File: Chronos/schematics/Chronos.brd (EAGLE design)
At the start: 61.6 x 100 mm, 72 parts, among them IC1 REG1117, IC4 QUAD_OPAMPD, Q301 BC846, Q701 BC846, U1 STM32F10XRXT6

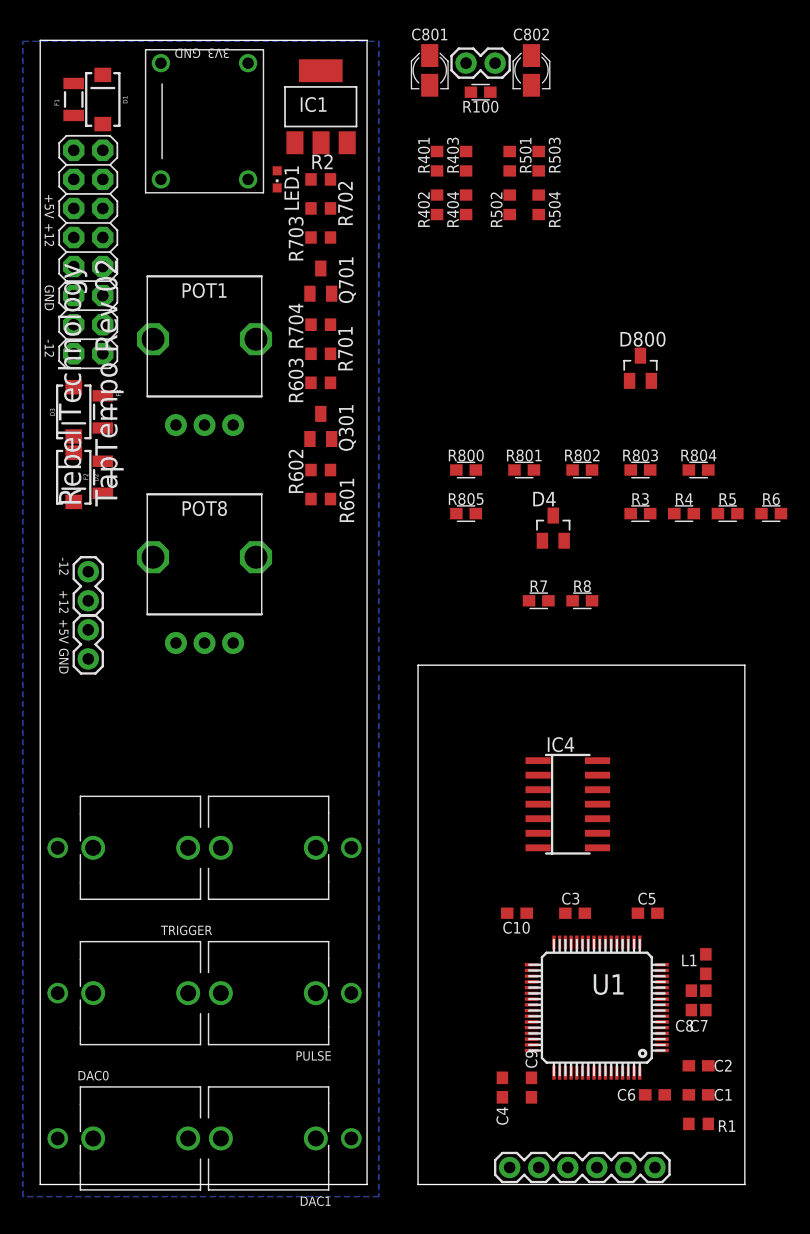
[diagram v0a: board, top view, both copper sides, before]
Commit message: replaced Chronos with TapTempoMk2
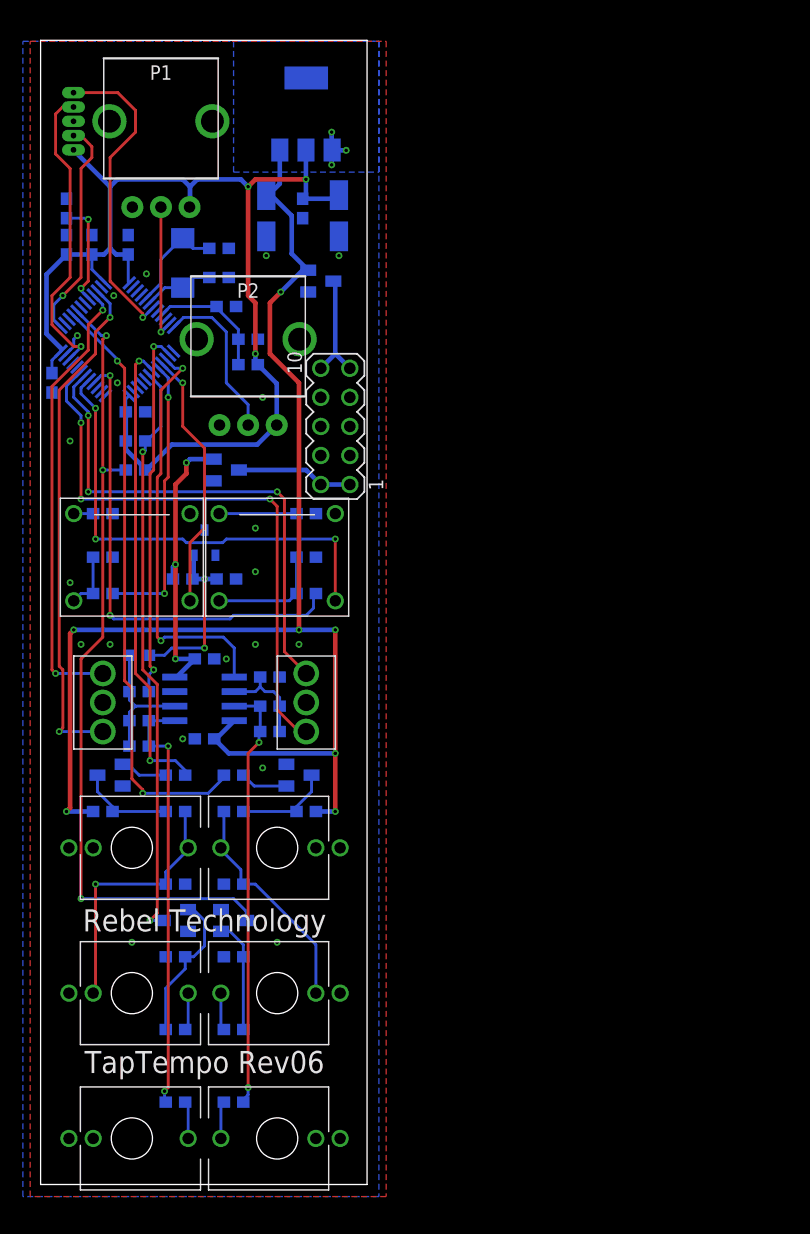
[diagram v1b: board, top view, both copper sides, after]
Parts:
- removed C801, C802: 10u, resistor:PANASONIC_A
- removed D1, D2, D3: (no value), SparkFun:SMA-DIODE
- removed D4, D800: BAT54S, diode:SOT23
- removed DAC0: THONKICONN, Rebel:THONKICONN
- removed F1, F2, F3: PTCSMD, SparkFun:PTC-1206
- removed IC4: QUAD_OPAMPD, adafruit:SO14
- removed JP1: (no value), SparkFun:1X06
- removed JP21, JP22, JP23: (no value), SparkFun:1X02
- removed LED1: (no value), led:CHIPLED_0603
- removed POT1, POT8: POT-ALPS-RK09L1140, Rebel:POT-ALPS-RK09L1140
- removed Q301, Q701: BC846, transistor:SOT23
- removed R100: 150R, Rebel:0603
- removed R401: 270k, resistor:R0603
- removed R402, R502: 100k, resistor:R0603
- removed R403, R503: 68k, resistor:R0603
- removed R404, R504: 100R, resistor:R0603
- removed R501: 470k, resistor:R0603
- removed R601: 100K, resistor:R0603
- removed R602: 1M, resistor:R0603
- removed R603: 10K, resistor:R0603
- removed R701, R702, R704: 1K, resistor:R0603
- removed R703: 100, resistor:R0603
- removed R800, R802: 240k, Rebel:0603
- removed R801: 100k, Rebel:0603
- removed R803: 68k, Rebel:0603
- removed R804: 1k, Rebel:0603
- removed R805: 100R, Rebel:0603
- removed U$1: 5GTH9, SWITCH-5GTH9:5GTH9
- removed U$2: M08X2, SparkFun:2X8
- removed U$3: (no value), Rebel:RT-LOGO-35MM-BL
- added C11, C13, C14, C16, C18, C19: 100n, Rebel:C0603
- added C12, C17: 10u, Rebel:153CLV-0405
- added C15: 1u, Rebel:C0603
- added DAC2: THONKICONN, Rebel:THONKICONN
- added IC2: TL072D, linear:SO08
- added IC3: LM4040B10, texas:DBZ_R-PDSO-G3
- added P1, P2: POT-ALPS-RK09L1140, Rebel:POT-ALPS-RK09L1140
- added PUSH1, PUSH2: 5GTH9, SWITCH-5GTH9:5GTH9
- added Q4: SI2309CDS, transistor-small-signal:SOT23
- added Q5: BSS123, transistor-small-signal:SOT23
- added R10, R13, R16, R17: 1K, Rebel:0603
- added R11: 100K, Rebel:0603
- added R12, R26, R27: 100R, Rebel:0603
- added R14: 1M, Rebel:0603
- added R15, R9: 10K, Rebel:0603
- added R18, R19: 150R, Rebel:0603
- added R20, R23: 1k, Rebel:0603
- added R21: 510R, Rebel:0603
- added R22: 6k8, Rebel:0603
- added R24: 3k3, Rebel:0603
- added R25: 2k, Rebel:0603
- added SV1: (no value), con-lstb:MA05-2
- added SW1, SW2: SUB-MIN-SPDT, Rebel:SUB-MIN-SPDT
- added T1, T2, T3, T4: BC846, transistor:SOT23
- added X1: 53048-05, con-molex:53048-05
- added Y1: 8MHz, Seeed-OPL-crystal-osctllator:X2-SMD-5.0X3.2X1.3MM
- C1: value 1u -> 2u2; device resistor:C0603 -> Rebel:C0603
- C10, C2, C5, C9: device resistor:C0603 -> Rebel:C0603
- C3: value 2u2 -> 4.7u; device resistor:C0603 -> Rebel:C0603
- C4: value 2u2 -> 100n; device resistor:C0603 -> Rebel:C0603
- C6, C8: value 100n -> 20pF; device resistor:C0603 -> Rebel:C0603
- C7: value 1u -> 100n; device resistor:C0603 -> Rebel:C0603
- IC1: value REG1117 -> TLV1117-33CDCY
- L1: device Rebel:0603@1 -> Rebel:0603
- R1: value 10K -> 1K; device resistor:R0603 -> Rebel:0603
- R2: device resistor:R0603 -> Rebel:0603
- R3: value 100k -> 100K
- R4: value 240k -> 100R
- R5: value 240k -> 1K
- R6: value 68k -> 1M
- R7: value 1k -> 10K
- R8: value 100R -> 1K
- U1: value STM32F10XRXT6 -> STM32F100CBT6B; device stm32:TQFP64 -> Rebel:QFP50P900X900X160-48N
- moved C6 83.2 mm to (17.8, 82.9), flipped to the bottom
- moved C9 83.1 mm to (6.67, 83.2), flipped to the bottom, turned to 90 degrees
- moved C2 78.1 mm to (18.4, 77.8), flipped to the bottom, turned to 180 degrees
- moved C1 76.9 mm to (20.3, 74.9), flipped to the bottom, turned to 180 degrees
- moved C8 75.5 mm to (17.8, 80.3), flipped to the bottom, turned to 180 degrees
- moved C3 73.4 mm to (4.45, 83.2), flipped to the bottom, turned to 90 degrees
- moved U1 71.9 mm to (8.89, 74.9), flipped to the bottom, turned to 315 degrees
- moved C7 71.6 mm to (10.5, 68.6), flipped to the bottom, turned to 180 degrees
- moved L1 65.9 mm to (20.3, 72.7), flipped to the bottom, turned to 0 degrees
- moved C10 61.6 mm to (3.17, 71.1), flipped to the bottom, turned to 270 degrees
- moved R6 60.9 mm to (19.1, 21.0), flipped to the bottom
- moved R3 57.4 mm to (19.1, 14.6), flipped to the bottom, turned to 180 degrees
- moved C5 56.9 mm to (7.62, 55.9), flipped to the bottom, turned to 180 degrees
- moved R2 55.3 mm to (25.4, 33.7), flipped to the bottom
- moved R5 54.0 mm to (19.1, 27.3), flipped to the bottom, turned to 180 degrees
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- renumbered PULSE to TEMPO2, TRIGGER to TEMPO1, TRIGGER1 to TR2, TRIGGER2 to TR1
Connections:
- removed net +5V: C801.+, D1.C, F1.2, IC1.3, JP22.1
- removed net ADC3: U1.9
- removed net ADC4: R8.1, R805.1, U1.15
- removed net ADC5: U1.16
- removed net ADC6: U1.8
- removed net DI0: Q301.3, R603.2, U1.50
- removed net DI1: U1.28
- removed net DO0: R701.1, U1.57
- removed net DO1: U1.27
- removed net N$19: LED1.C, R2.2
- removed net N$29: DAC1.P$2
- removed net N$33: IC4.2, R800.2, R801.2, R802.2, R803.1
- removed net N$35: R703.2, R704.2, TEMPO2.P$3
- removed net N$36: D800.3, R804.1, R805.2
- removed net N$44: F1.1, U$2.11, U$2.12
- removed net N$45: F2.1, U$2.10, U$2.9
- removed net N$8: DAC0.P$2
- removed net PA0: U1.14
- removed net PA10: U1.43
- removed net PA11: U1.44
- removed net PA12: U1.45
- removed net PA3: U1.17
- removed net PA4: R403.2, U1.20
- removed net PA5: R503.2, U1.21
- removed net PA6: U1.22
- removed net PA7: U1.23
- removed net PA8: U1.41
- removed net PA9: U1.42
- removed net PB0: U1.26
- removed net PB10: U1.29
- removed net PB11: U1.30
- removed net PB12: U1.33
- removed net PB13: U1.34
- removed net PB14: U1.35
- removed net PB15: U1.36
- removed net PB4: U1.56
- removed net PB6: U1.58
- removed net PB7: U1.59
- removed net PB8: U1.61
- removed net PB9: U1.62
- removed net PC10: U1.51
- removed net PC11: U1.52
- removed net PC12: U1.53
- removed net PC13: U1.2
- removed net PC14: U1.3
- removed net PC15: U1.4
- removed net PC4: U1.24
- removed net PC5: U1.25
- removed net PC6: U1.37
- removed net PC7: U1.38
- removed net PC8: U1.39
- removed net PC9: U1.40
- removed net PD2: U1.54
- removed net PE2: U$1.4
- removed net PE3: R100.2
- removed net PE5: U$1.-2
- removed net SWO: JP1.6, U1.55
- removed net VCAP_1: C3.1, U1.31
- removed net VCAP_2: C4.1, U1.47
- new net BOOT1: U1.20
- new net CV_REF: C16.1, IC3.2, R21.2, R22.2
- new net DAC1: R23.2, U1.14
- new net DAC2: IC2.5, U1.15
- new net LED1: PUSH1.+3, U1.16
- new net LED2: PUSH2.+3, U1.29
- new net N$15: R4.2, R5.2, TEMPO2.P$2, TR2.P$3
- new net N$16: Q5.3, SV1.1, SV1.2
- new net N$17: C5.1, PUSH1.4, R17.1
- new net OSC_IN: C6.1, U1.5, Y1.1
- new net PUSH1: R17.2, U1.17
- new net PUSH2: R16.2, U1.28
- new net SW1A: SW1.3, U1.45
- new net SW1B: SW1.1, U1.46
- new net SW2A: SW2.3, U1.30
- new net SW2B: SW2.1, U1.31
- new net TEMPO1: R15.2, T4.3, U1.19
- new net TEMPO2: R7.2, T2.3, U1.41
- new net TR1: R8.1, U1.18
- new net TR2: R1.1, U1.40
- net +12V: now also C12.+, C19.1, IC1.3, IC2.8, Q4.2, R10.1, R2.1; no longer D2.C, F2.2, IC4.4, JP23.1, POT1.3, POT8.3, R702.1
- net +3V3: now also C11.1, C15.1, C17.+, C3.1, C7.1, IC1.4, L1.1, P1.3, P2.3, R15.1, R7.1, U1.24, U1.36, X1.1; no longer C1.1, C2.1, C5.1, C6.1, C802.+, D4.2, D800.2, JP1.1, JP21.1, L1.2, LED1.A, R603.1, U1.19, U1.32, U1.64
- net -12V: now also C18.1, IC2.4, Q5.2, R21.1; no longer D3.A, F3.2, IC4.11, JP23.2, R401.2, R5.1, R501.2, R802.1
- net ADC1: now also P1.2
- net ADC2: now also P2.2, U1.12; no longer U1.10
- net BOOT0: now also R9.1, U1.44; no longer R1.1, U1.60
- net GND: now also C11.2, C12.-, C15.2, C16.2, C17.-, C18.2, C19.2, DAC2.P$1, IC2.3, IC3.1, P1.1, P1.P$5, P1.P$6, P2.1, P2.P$5, P2.P$6, PUSH1.1, PUSH2.1, Q4.1, Q5.1, R13.1, R14.2, R18.2, R19.2, R20.1, R5.1, R6.2, R9.2, SV1.3, SV1.4, SV1.5, SV1.6, SV1.7, SV1.8, SW1.2, SW2.2, T1.2, T2.2, T3.2, T4.2, U1.23, U1.35, U1.47, U1.8, X1.3; no longer C801.-, C802.-, D1.A, D2.A, D3.C, D4.1, D800.1, DAC0.P$1, IC4.12, IC4.3, IC4.6, IC4.9, JP1.3, JP21.2, JP22.2, POT1.1, POT8.1, Q301.2, Q701.2, R1.2, R2.1, R602.2, R704.1, TEMPO1.P$2, TR1.P$2, TR2.P$2, U$1.1, U$2.3, U$2.4, U$2.5, U$2.6, U$2.7, U$2.8, U1.12, U1.18, U1.63
- net N$1: now also C8.1, U1.6, Y1.2; no longer R801.1, TR2.P$3
- net N$10: now also R3.2, R6.1, T2.1; no longer R100.1, U$1.+3
- net N$11: now also R1.2, T1.1; no longer POT1.2, R4.1
- net N$12: now also R2.2, R4.1, T1.3; no longer IC4.14, R6.2, R7.2
- net N$13: now also C13.1, IC2.2, R22.1, R23.1, R24.1; no longer IC4.5, R401.1, R402.1, R403.1
- net N$14: now also R3.1, TEMPO2.P$3; no longer D4.3, R7.1, R8.2
- net N$18: now also C4.1, PUSH2.4, R16.1; no longer IC4.10, R501.1, R502.1, R503.1
- net N$2: now also PUSH1.-2, R19.1; no longer POT8.2, R800.1
- net N$23: now also R11.1; no longer R601.1
- net N$27: now also R11.2, R14.1, T4.1; no longer Q301.1, R601.2, R602.1
- net N$3: now also C14.2, IC2.7, R25.2, R27.1; no longer IC4.1, R803.2, R804.2
- net N$31: now also DAC1.P$3, R26.2; no longer DAC0.P$3, R404.2
- net N$32: now also DAC2.P$3, R27.2; no longer DAC1.P$3, R504.2
- net N$34: now also R8.2, T3.1; no longer Q701.1, R701.2
- net N$38: now also R10.2, R12.1, T3.3; no longer Q701.3, R702.2, R703.1
- net N$4: now also C14.1, IC2.6, R20.2, R25.1; no longer R3.1, TR1.P$3
- net N$5: now also R12.2, R13.2, TEMPO1.P$2, TR1.P$3; no longer IC4.8, R502.2, R504.1
- net N$6: now also Q4.3, SV1.10, SV1.9; no longer F3.1, U$2.1, U$2.2
- net N$7: now also C13.2, IC2.1, R24.2, R26.1; no longer IC4.7, R402.2, R404.1
- net N$9: now also PUSH2.-2, R18.1; no longer IC4.13, R3.2, R4.2, R5.2, R6.1
- net NRST: now also X1.5; no longer JP1.5
- net SWCLK: now also U1.37, X1.2; no longer JP1.2, U1.49
- net SWDIO: now also U1.34, X1.4; no longer JP1.4, U1.46
- net VDDA: now also C1.1, C2.1, L1.2, U1.9; no longer C7.1, C8.1, L1.1, U1.13
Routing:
- net +12V: track 0.00 -> 119.4 mm, vias 0 -> 7
- net +3V3: track 0.00 -> 104.0 mm, vias 0 -> 3
- net TEMPO2: track 0.00 -> 71.3 mm, vias 0 -> 3
- net TR2: track 0.00 -> 52.2 mm, vias 0 -> 2
- net SW2B: track 0.00 -> 50.7 mm, vias 0 -> 3
- net TEMPO1: track 0.00 -> 50.7 mm, vias 0 -> 2
- net SW1B: track 0.00 -> 44.9 mm, vias 0 -> 2
- net SW2A: track 0.00 -> 44.6 mm, vias 0 -> 3
- net PUSH2: track 0.00 -> 42.4 mm, vias 0 -> 2
- net LED2: track 0.00 -> 41.4 mm, vias 0 -> 3
- net TR1: track 0.00 -> 41.1 mm, vias 0 -> 2
- net SW1A: track 0.00 -> 39.5 mm, vias 0 -> 2
- net N$7: track 0.00 -> 37.5 mm, vias 0 -> 2
- net N$3: track 0.00 -> 37.5 mm, vias 0 -> 2
- net DAC2: track 0.00 -> 36.2 mm, vias 0 -> 2
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- added copper zone on layer 16, net +3V3
- added copper zone on layer 1, net GND
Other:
- board size 61.6 x 100 mm -> 28.5 x 100 mm
- board text added: "-12v"
- board text added: "TapTempo Rev06"
- board text removed: "+12"
- board text removed: "+5V"
- board text removed: "-12"
- board text removed: "3V3"
- board text removed: "GND"
- board text removed: "TapTempo Rev 02"

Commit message: Increased cap size to 5mm 47uF. Added logo. Rev07.
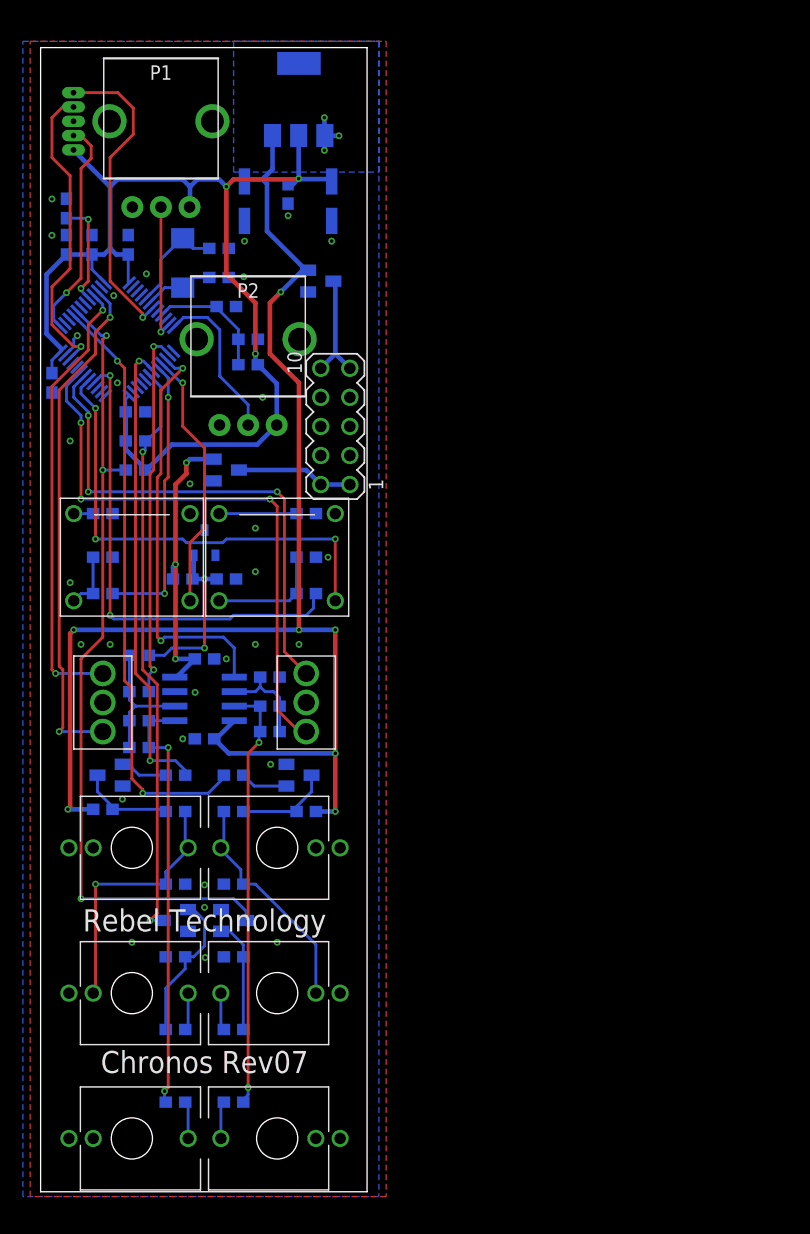
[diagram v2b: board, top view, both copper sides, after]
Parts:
- C12, C17: value 10u -> 47u; device Rebel:153CLV-0405 -> Rebel:CPOL-5
- moved C12 2.29 mm to (20.0, 87.0)
- moved C15 1.80 mm to (23.8, 87.6)
- moved C17 1.42 mm to (27.6, 87.0)
- moved IC1 1.42 mm to (24.8, 95.9)
- moved R10 0.19 mm to (7.62, 33.8)
- moved C13 0.13 mm to (10.8, 39.2)
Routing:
- net +12V: track 119.4 -> 121.8 mm
- net GND: track 6.35 -> 6.33 mm, vias 23 -> 34
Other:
- board text added: "Chronos Rev07"
- board text removed: "TapTempo Rev06"
